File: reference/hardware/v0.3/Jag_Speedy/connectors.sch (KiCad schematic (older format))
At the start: 5 parts, among them J1 Inputs, J2 Ouputs01, J3 Outputs02, J4 Power, J5 Bluetooth

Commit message: Schematic pin mapping
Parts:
- added J7: Canbus, Connector_PinHeader_1.00mm:PinHeader_1x06_P1.00mm_Horizontal, symbol Connector_Generic:Conn_01x06
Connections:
- net 5V: now also J7.2 (Pin_2)
- net GND: now also J7.1 (Pin_1)
- new net CAN-Rx: J7.4 (Pin_4)
- new net CAN-Tx: J7.3 (Pin_3)
- no-connect marks 6 -> 8

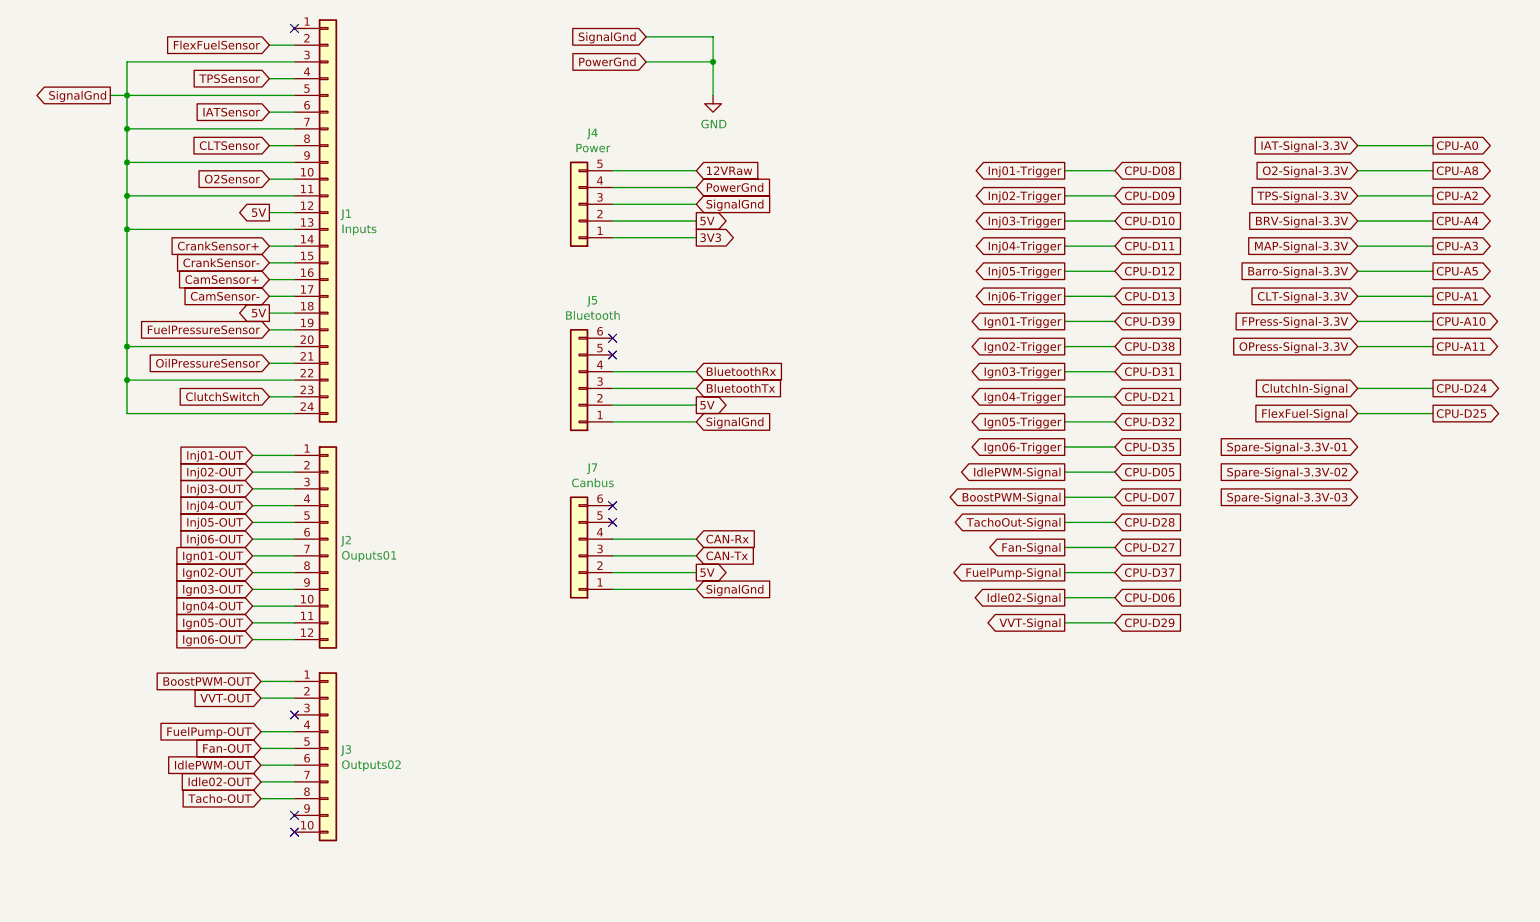
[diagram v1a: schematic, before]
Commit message: Canbus Tranceiver
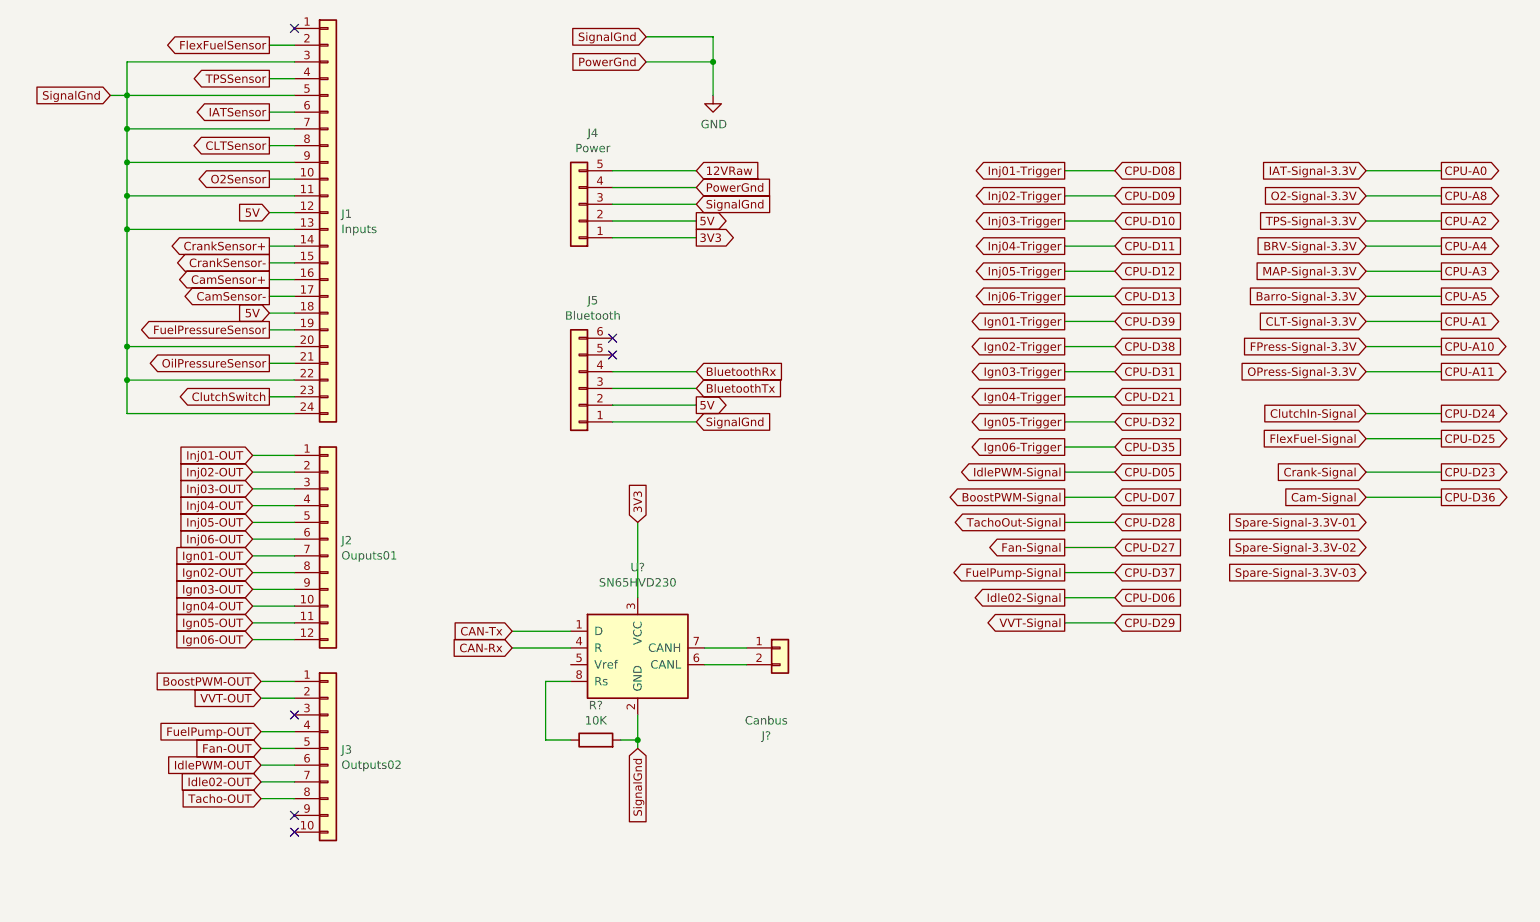
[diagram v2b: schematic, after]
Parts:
- removed J7: Canbus, Connector_PinHeader_1.00mm:PinHeader_1x06_P1.00mm_Horizontal, symbol Connector_Generic:Conn_01x06
- added J?: Canbus, Connector_PinHeader_1.00mm:PinHeader_1x06_P1.00mm_Horizontal, symbol Connector_Generic:Conn_01x02
- added R?: 10K, symbol Device:R
- added U?: SN65HVD230, Package_SO:SOIC-8_3.9x4.9mm_P1.27mm, symbol Interface_CAN_LIN:SN65HVD230
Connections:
- net 3V3: now also U?.3 (VCC)
- net CAN-Rx: now also U?.4 (R)
- net CAN-Tx: now also U?.1 (D)
- net GND: now also R?.2, U?.2 (GND)
- new net: J?.2 (Pin_2), U?.6 (CANL)
- new net: J?.1 (Pin_1), U?.7 (CANH)
- new net: R?.1, U?.8 (Rs)
- no-connect marks 8 -> 6
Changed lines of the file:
@@
 	1    0    0    -1
 $EndComp
-Text GLabel 2250 1200 0    50   Input ~ 0
+Text GLabel 2250 1200 0    50   Output ~ 0
 TPSSensor
-Text GLabel 2250 1400 0    50   Input ~ 0
+Text GLabel 2250 1400 0    50   Output ~ 0
 IATSensor
-Text GLabel 2250 1600 0    50   Input ~ 0
+Text GLabel 2250 1600 0    50   Output ~ 0
 CLTSensor
-Text GLabel 2250 1800 0    50   Input ~ 0
+Text GLabel 2250 1800 0    50   Output ~ 0
 O2Sensor
-Text GLabel 2250 2200 0    50   Input ~ 0
+Text GLabel 2250 2200 0    50   Output ~ 0
 CrankSensor+
 $Comp
@@
 	-1   0    0    1
 $EndComp
-Text GLabel 2250 2400 0    50   Input ~ 0
+Text GLabel 2250 2400 0    50   Output ~ 0
 CamSensor+
-Text GLabel 2250 2700 0    50   Input ~ 0
+Text GLabel 2250 2700 0    50   Output ~ 0
 FuelPressureSensor
-Text GLabel 2250 2900 0    50   Input ~ 0
+Text GLabel 2250 2900 0    50   Output ~ 0
 OilPressureSensor
 $Comp
@@
 Text GLabel 2200 5300 0    50   Input ~ 0
 IdlePWM-OUT
-Text GLabel 2250 2000 0    50   Output ~ 0
+Text GLabel 2250 2000 0    50   Input ~ 0
 5V
-Text GLabel 2250 2600 0    50   Output ~ 0
+Text GLabel 2250 2600 0    50   Input ~ 0
 5V
 Wire Wire Line
@@
 Wire Wire Line
 	4300 1950 4800 1950
-Text GLabel 1300 1300 0    50   Output ~ 0
+Text GLabel 1300 1300 0    50   Input ~ 0
 SignalGnd
 Wire Wire Line
@@
 Wire Wire Line
 	4800 3050 4300 3050
-Text GLabel 2250 2300 0    50   Input ~ 0
+Text GLabel 2250 2300 0    50   Output ~ 0
 CrankSensor-
-Text GLabel 2250 2500 0    50   Input ~ 0
+Text GLabel 2250 2500 0    50   Output ~ 0
 CamSensor-
 Wire Wire Line
@@
 Wire Wire Line
 	4800 2150 4300 2150
-Text GLabel 2250 1000 0    50   Input ~ 0
+Text GLabel 2250 1000 0    50   Output ~ 0
 FlexFuelSensor
-Text GLabel 2250 3100 0    50   Input ~ 0
+Text GLabel 2250 3100 0    50   Output ~ 0
 ClutchSwitch
 Wire Wire Line
@@
 Wire Wire Line
 	7300 3400 7000 3400
-$Comp
-L Connector_Generic:Conn_01x06 J7
-U 1 1 5EFFD7CF
-P 4100 4050
-F 0 "J7" H 4018 3525 50  0000 C CNN
-F 1 "Canbus" H 4018 3616 50  0000 C CNN
-F 2 "Connector_PinHeader_1.00mm:PinHeader_1x06_P1.00mm_Horizontal" H 4100 4050 50  0001 C CNN
-F 3 "~" H 4100 4050 50  0001 C CNN
-	1    4100 4050
-	-1   0    0    1
-$EndComp
-Text GLabel 4800 4250 2    50   Input ~ 0
-SignalGnd
-Text GLabel 4800 4050 2    50   Input ~ 0
-CAN-Tx
-Text GLabel 4800 3950 2    50   Input ~ 0
-CAN-Rx
-Text GLabel 4800 4150 2    50   Output ~ 0
-5V
-Wire Wire Line
-	4300 3950 4800 3950
-Wire Wire Line
-	4800 4050 4300 4050
-Wire Wire Line
-	4300 4150 4800 4150
-Wire Wire Line
-	4800 4250 4300 4250
-NoConn ~ 4300 3750
-NoConn ~ 4300 3850
 Text GLabel 7000 3550 0    50   Output ~ 0
 IdlePWM-Signal
@@
 Wire Wire Line
 	7300 4450 7000 4450
-Text GLabel 8750 1750 0    50   Input ~ 0
+Text GLabel 8800 1900 0    50   Input ~ 0
 O2-Signal-3.3V
-Text GLabel 9200 1750 2    50   Output ~ 0
+Text GLabel 9250 1900 2    50   Output ~ 0
 CPU-A8
-Text GLabel 8750 1900 0    50   Input ~ 0
+Text GLabel 8800 2050 0    50   Input ~ 0
 TPS-Signal-3.3V
-Text GLabel 9200 1900 2    50   Output ~ 0
+Text GLabel 9250 2050 2    50   Output ~ 0
 CPU-A2
-Text GLabel 8750 2050 0    50   Input ~ 0
+Text GLabel 8800 2200 0    50   Input ~ 0
 BRV-Signal-3.3V
-Text GLabel 9200 2050 2    50   Output ~ 0
+Text GLabel 9250 2200 2    50   Output ~ 0
 CPU-A4
-Text GLabel 8750 2200 0    50   Input ~ 0
+Text GLabel 8800 2350 0    50   Input ~ 0
 MAP-Signal-3.3V
-Text GLabel 9200 2200 2    50   Output ~ 0
+Text GLabel 9250 2350 2    50   Output ~ 0
 CPU-A3
-Text GLabel 8750 2350 0    50   Input ~ 0
+Text GLabel 8800 2500 0    50   Input ~ 0
 Barro-Signal-3.3V
-Text GLabel 9200 2350 2    50   Output ~ 0
+Text GLabel 9250 2500 2    50   Output ~ 0
 CPU-A5
-Text GLabel 8750 2500 0    50   Input ~ 0
+Text GLabel 8800 2650 0    50   Input ~ 0
 CLT-Signal-3.3V
-Text GLabel 9200 2500 2    50   Output ~ 0
+Text GLabel 9250 2650 2    50   Output ~ 0
 CPU-A1
-Text GLabel 8750 2650 0    50   Input ~ 0
+Text GLabel 8800 2800 0    50   Input ~ 0
 FPress-Signal-3.3V
-Text GLabel 9200 2650 2    50   Output ~ 0
+Text GLabel 9250 2800 2    50   Output ~ 0
 CPU-A10
-Text GLabel 8750 2800 0    50   Input ~ 0
+Text GLabel 8800 2950 0    50   Input ~ 0
 OPress-Signal-3.3V
-Text GLabel 9200 2800 2    50   Output ~ 0
+Text GLabel 9250 2950 2    50   Output ~ 0
 CPU-A11
-Text GLabel 8750 3200 0    50   Input ~ 0
+Text GLabel 8800 3350 0    50   Input ~ 0
 FlexFuel-Signal
-Text GLabel 8750 3050 0    50   Input ~ 0
+Text GLabel 8800 3200 0    50   Input ~ 0
 ClutchIn-Signal
-Text GLabel 9200 3050 2    50   Output ~ 0
+Text GLabel 9250 3200 2    50   Output ~ 0
 CPU-D24
-Text GLabel 9200 3200 2    50   Output ~ 0
+Text GLabel 9250 3350 2    50   Output ~ 0
 CPU-D25
 Wire Wire Line
-	8750 1750 9200 1750
-Wire Wire Line
-	9200 1900 8750 1900
-Wire Wire Line
-	8750 2050 9200 2050
-Wire Wire Line
-	9200 2200 8750 2200
-Wire Wire Line
-	8750 2350 9200 2350
-Wire Wire Line
-	9200 2500 8750 2500
-Wire Wire Line
-	8750 2650 9200 2650
-Wire Wire Line
-	9200 2800 8750 2800
-Wire Wire Line
-	8750 3050 9200 3050
-Wire Wire Line
-	9200 3200 8750 3200
-Text GLabel 8750 3550 0    50   Input ~ 0
+	8800 1900 9250 1900
+Wire Wire Line
+	9250 2050 8800 2050
+Wire Wire Line
+	8800 2200 9250 2200
+Wire Wire Line
+	9250 2350 8800 2350
+Wire Wire Line
+	8800 2500 9250 2500
+Wire Wire Line
+	9250 2650 8800 2650
+Wire Wire Line
+	8800 2800 9250 2800
+Wire Wire Line
+	9250 2950 8800 2950
+Wire Wire Line
+	8800 3200 9250 3200
+Wire Wire Line
+	9250 3350 8800 3350
+Text GLabel 8800 4000 0    50   Input ~ 0
 Spare-Signal-3.3V-02
-Text GLabel 8750 3700 0    50   Input ~ 0
+Text GLabel 8800 4150 0    50   Input ~ 0
 Spare-Signal-3.3V-03
-Text GLabel 8750 3400 0    50   Input ~ 0
+Text GLabel 8800 3850 0    50   Input ~ 0
 Spare-Signal-3.3V-01
-Text GLabel 8750 1600 0    50   Input ~ 0
+Text GLabel 8800 1750 0    50   Input ~ 0
 IAT-Signal-3.3V
-Text GLabel 9200 1600 2    50   Output ~ 0
+Text GLabel 9250 1750 2    50   Output ~ 0
 CPU-A0
 Wire Wire Line
-	8750 1600 9200 1600
+	8800 1750 9250 1750
+Text GLabel 8800 3550 0    50   Input ~ 0
+Crank-Signal
+Text GLabel 8800 3700 0    50   Input ~ 0
+Cam-Signal
+Text GLabel 9250 3700 2    50   Output ~ 0
+CPU-D36
+Text GLabel 9250 3550 2    50   Output ~ 0
+CPU-D23
+Wire Wire Line
+	8800 3700 9250 3700
+Wire Wire Line
+	9250 3550 8800 3550
+$Comp
+L Interface_CAN_LIN:SN65HVD230 U?
+U 1 1 5F25636D
+P 4450 4600
+AR Path="/5F25636D" Ref="U?"  Part="1"
+AR Path="/5EF0527D/5F25636D" Ref="U?"  Part="1"
+F 0 "U?" H 4450 5081 50  0000 C CNN
+F 1 "SN65HVD230" H 4450 4990 50  0000 C CNN
+F 2 "Package_SO:SOIC-8_3.9x4.9mm_P1.27mm" H 4450 4100 50  0001 C CNN
+F 3 "http://www.ti.com/lit/ds/symlink/sn65hvd230.pdf" H 4350 5000 50  0001 C CNN
+	1    4450 4600
+	1    0    0    -1
+$EndComp
+Text GLabel 3700 4500 0    50   Input ~ 0
+CAN-Tx
+Text GLabel 3700 4600 0    50   Input ~ 0
+CAN-Rx
+Text GLabel 4450 3850 1    50   Input ~ 0
+3V3
+Text GLabel 4450 5200 3    50   Input ~ 0
+SignalGnd
+$Comp
+L Connector_Generic:Conn_01x02 J?
+U 1 1 5F25E793
+P 5300 4600
+F 0 "J?" H 5218 4075 50  0000 C CNN
+F 1 "Canbus" H 5218 4166 50  0000 C CNN
+F 2 "Connector_PinHeader_1.00mm:PinHeader_1x06_P1.00mm_Horizontal" H 5300 4600 50  0001 C CNN
+F 3 "~" H 5300 4600 50  0001 C CNN
+	1    5300 4600
+	1    0    0    -1
+$EndComp
+$Comp
+L Device:R R?
+U 1 1 5F25F382
+P 4200 5150
+F 0 "R?" V 4407 5150 50  0000 C CNN
+F 1 "10K" V 4316 5150 50  0000 C CNN
+F 2 "" V 4130 5150 50  0001 C CNN
+F 3 "~" H 4200 5150 50  0001 C CNN
+	1    4200 5150
+	0    -1   -1   0
+$EndComp
+Wire Wire Line
+	4450 5200 4450 5150
+Wire Wire Line
+	4450 3850 4450 4300
+Wire Wire Line
+	3700 4500 4050 4500
+Wire Wire Line
+	4050 4600 3700 4600
+Wire Wire Line
+	4050 5150 3900 5150
+Wire Wire Line
+	3900 5150 3900 4800
+Wire Wire Line
+	3900 4800 4050 4800
+Wire Wire Line
+	4350 5150 4450 5150
+Connection ~ 4450 5150
+Wire Wire Line
+	4450 5150 4450 5000
+Wire Wire Line
+	4850 4700 5100 4700
+Wire Wire Line
+	5100 4600 4850 4600
 $EndSCHEMATC

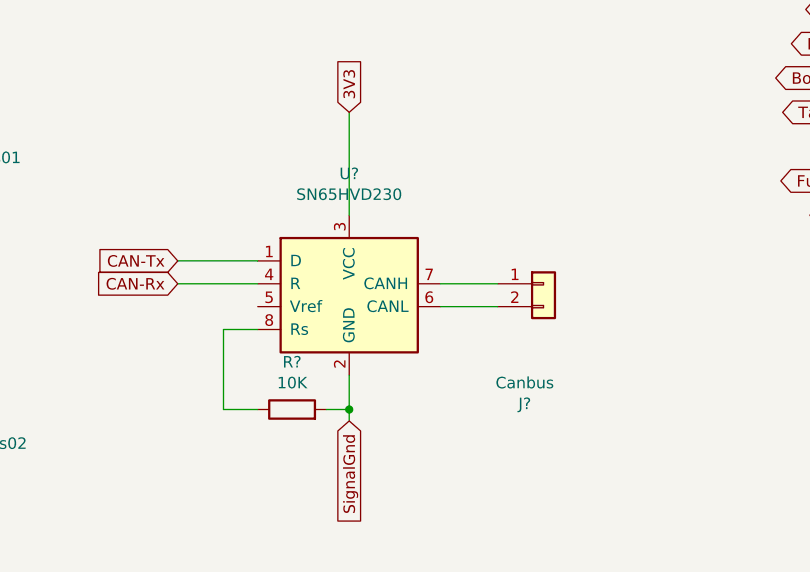
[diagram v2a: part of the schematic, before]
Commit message: Driver replacement
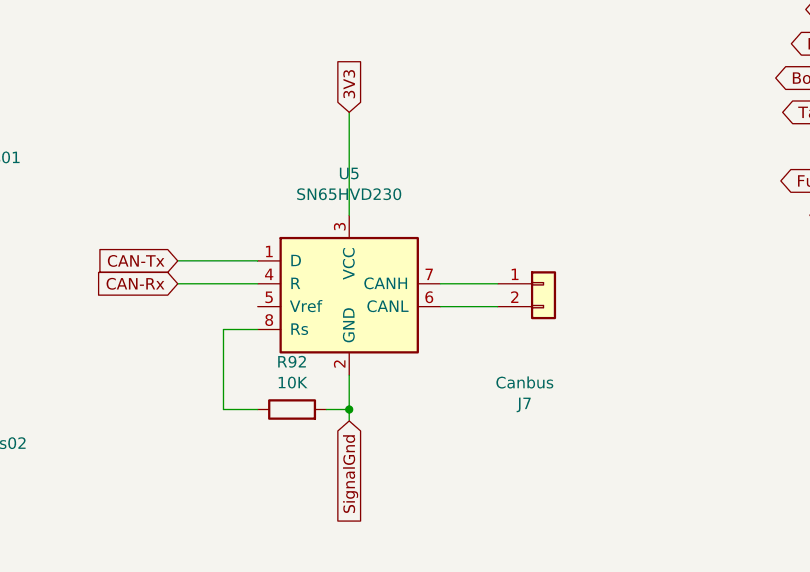
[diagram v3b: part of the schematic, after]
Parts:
- gave numbers to parts that had none: 3
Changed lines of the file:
@@
 P 4450 4600
 AR Path="/5F25636D" Ref="U?"  Part="1"
-AR Path="/5EF0527D/5F25636D" Ref="U?"  Part="1"
-F 0 "U?" H 4450 5081 50  0000 C CNN
+AR Path="/5EF0527D/5F25636D" Ref="U5"  Part="1"
+F 0 "U5" H 4450 5081 50  0000 C CNN
 F 1 "SN65HVD230" H 4450 4990 50  0000 C CNN
 F 2 "Package_SO:SOIC-8_3.9x4.9mm_P1.27mm" H 4450 4100 50  0001 C CNN
@@
 SignalGnd
 $Comp
-L Connector_Generic:Conn_01x02 J?
+L Connector_Generic:Conn_01x02 J7
 U 1 1 5F25E793
 P 5300 4600
-F 0 "J?" H 5218 4075 50  0000 C CNN
+F 0 "J7" H 5218 4075 50  0000 C CNN
 F 1 "Canbus" H 5218 4166 50  0000 C CNN
 F 2 "Connector_PinHeader_1.00mm:PinHeader_1x06_P1.00mm_Horizontal" H 5300 4600 50  0001 C CNN
@@
 $EndComp
 $Comp
-L Device:R R?
+L Device:R R92
 U 1 1 5F25F382
 P 4200 5150
-F 0 "R?" V 4407 5150 50  0000 C CNN
+F 0 "R92" V 4407 5150 50  0000 C CNN
 F 1 "10K" V 4316 5150 50  0000 C CNN
 F 2 "" V 4130 5150 50  0001 C CNN

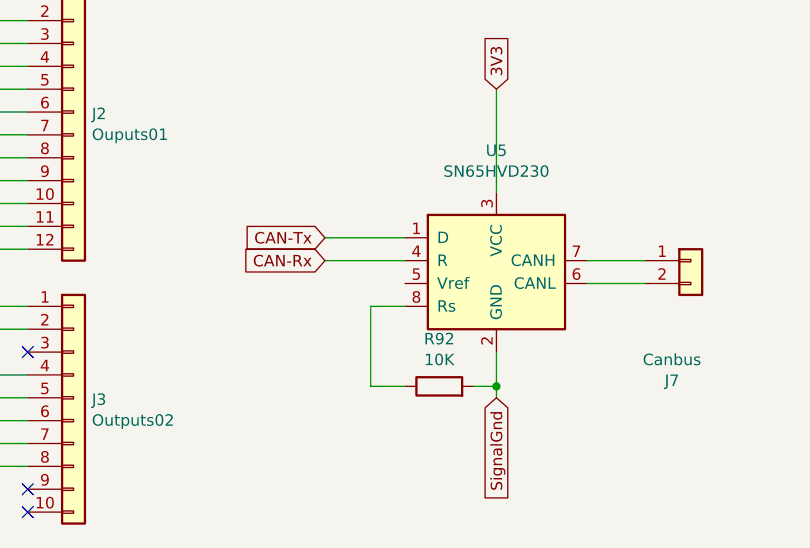
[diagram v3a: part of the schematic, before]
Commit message: MOSFET Drivers
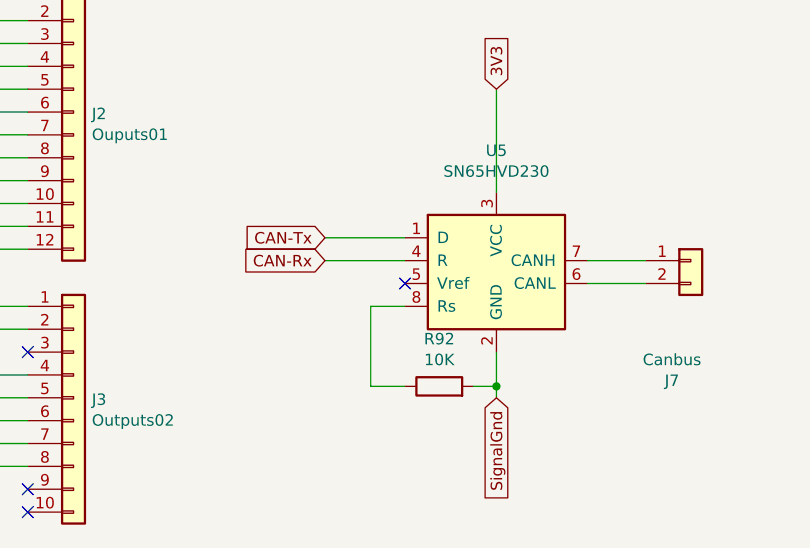
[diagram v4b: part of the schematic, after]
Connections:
- no-connect marks 6 -> 7
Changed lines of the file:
@@
 Wire Wire Line
 	5100 4600 4850 4600
+NoConn ~ 4050 4700
 $EndSCHEMATC
